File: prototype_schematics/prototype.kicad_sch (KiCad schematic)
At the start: 98 parts, among them J1 AudioJack3, J2 Conn_01x04, J3 Conn_Coaxial, U1 MAX2608EUT+T, U10 TA0411A, U2 SPX3819M5-L, U3 TLV61046ADB, U4 MAX2680AUT+, U5 CD74HC4046A, U6 BGA2802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

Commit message: layout wip
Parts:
- J3: footprint Connector_Coaxial:SMA_Wurth_60312002114503_Vertical -> Connector_Coaxial:SMA_Samtec_SMA-J-P-X-ST-EM1_EdgeMount; Digikey (none) -> CON-SMA-EDGE-S-ND
- L12: footprint Inductor_SMD:L_0201_0603Metric_Pad0.64x0.40mm_HandSolder -> Inductor_SMD:L_0603_1608Metric_Pad1.05x0.95mm_HandSolder
- TP1, TP2, TP3, TP4, TP5, TP6: footprint CONMHF1_SMD_T:CONN_CONMHF1-SMD_LNX -> Connector_Coaxial:U.FL_Molex_MCRF_73412-0110_Vertical
- U6: footprint Package_TO_SOT_SMD:SOT-363_SC-70-6 -> Package_TO_SOT_SMD:SOT-363_SC-70-6_Handsoldering
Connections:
- net GND: now also R9.1; no longer R9.2
- net at C10.2, C13.1, L5.1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: no longer R9.1
- net at C9.2: now also U4.1 (LO); no longer TP1.1 (In)
- net at C1.2: now also TP1.1 (In); no longer U4.1 (LO)
- net at C13.2, U5.14 (SigIn): now also R9.2
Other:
- note removed: "Remove 2kR when using TP"
- moved on the sheet: C10, C13, L5, L6, R9, TP1, TP2

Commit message: wip layout
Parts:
- added C40: 1nF, Capacitor_SMD:C_0603_1608Metric_Pad1.08x0.95mm_HandSolder, symbol Device:C_Small
- J2: footprint Connector_JST:JST_PH_S4B-PH-K_1x04_P2.00mm_Horizontal -> Connector_PinHeader_2.54mm:PinHeader_1x04_P2.54mm_Vertical
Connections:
- net AFOUT_N: now also J2.3 (Pin_3); no longer J2.4 (Pin_4)
- net AFOUT_P: now also J2.4 (Pin_4); no longer J2.3 (Pin_3)
- net GND: now also R9.2; no longer R9.1
- net at C10.2, L5.1: now also C40.1; no longer C13.1, Y1.3 (OUT/IN)
- net at R18.1: now also RV3.1; no longer RV3.3
- net at R17.2: now also RV3.3; no longer RV3.1
- net at C13.2, U5.14 (SigIn): no longer R9.2
- new net: C13.1, C40.2, R9.1, Y1.3 (OUT/IN)
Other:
- moved on the sheet: C10, C13, L5, L6, R9, TP2

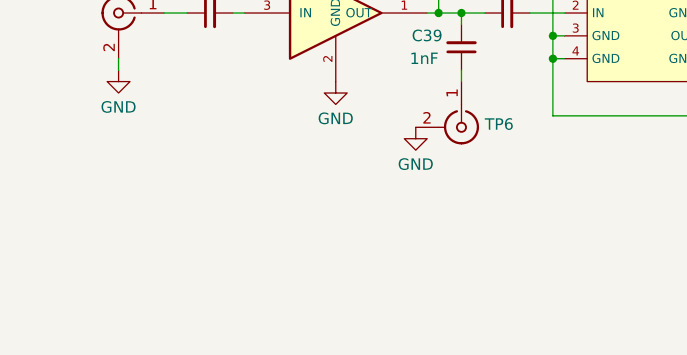
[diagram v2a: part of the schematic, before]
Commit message: layout adjustment and edge cut
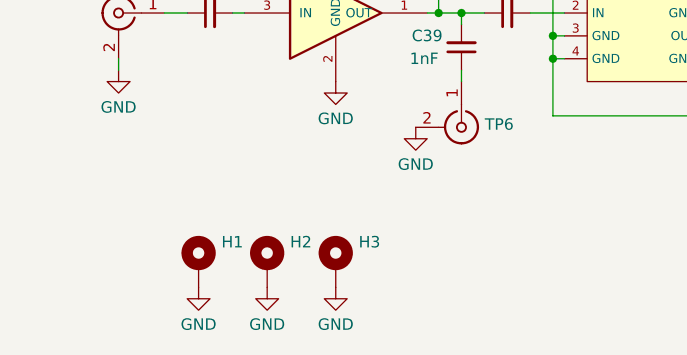
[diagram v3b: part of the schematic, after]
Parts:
- added H1, H2, H3: MountingHole_Pad, MountingHole:MountingHole_3.2mm_M3_Pad_TopBottom, symbol Mechanical:MountingHole_Pad
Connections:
- net GND: now also H1.1, H2.1, H3.1
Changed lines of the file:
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@@
     )
   )
+  (symbol (lib_id "Mechanical:MountingHole_Pad") (at 48.26 187.96 0) (unit 1)
+    (in_bom yes) (on_board yes) (dnp no) (fields_autoplaced)
+    (property "Reference" "H3" (at 50.8 185.4779 0)
+      (effects (font (size 1.27 1.27)) (justify left))
+    )
+    (property "Value" "MountingHole_Pad" (at 50.8 187.9021 0)
+      (effects (font (size 1.27 1.27)) (justify left) hide)
+    )
+    (property "Footprint" "MountingHole:MountingHole_3.2mm_M3_Pad_TopBottom" (at 48.26 187.96 0)
+      (effects (font (size 1.27 1.27)) hide)
+    )
+    (property "Datasheet" "~" (at 48.26 187.96 0)
+      (effects (font (size 1.27 1.27)) hide)
+    )
+    (pin "1")
+    (instances
+      (project "prototype"
+        (path "/4c96c703-bc8d-4d6a-931f-53feb2017a98"
+          (reference "H3") (unit 1)
+        )
+      )
+    )
+  )
   (symbol (lib_id "power:GND") (at 265.43 99.06 0) (unit 1)
     (in_bom yes) (on_board yes) (dnp no) (fields_autoplaced)
@@
     )
   )
+  (symbol (lib_id "power:GND") (at 48.26 190.5 0) (unit 1)
+    (in_bom yes) (on_board yes) (dnp no) (fields_autoplaced)
+    (property "Reference" "#PWR053" (at 48.26 196.85 0)
+      (effects (font (size 1.27 1.27)) hide)
+    )
+    (property "Value" "GND" (at 48.26 194.6331 0)
+      (effects (font (size 1.27 1.27)))
+    )
+    (property "Footprint" "" (at 48.26 190.5 0)
+      (effects (font (size 1.27 1.27)) hide)
+    )
+    (property "Datasheet" "" (at 48.26 190.5 0)
+      (effects (font (size 1.27 1.27)) hide)
+    )
+    (pin "1")
+    (instances
+      (project "prototype"
+        (path "/4c96c703-bc8d-4d6a-931f-53feb2017a98"
+          (reference "#PWR053") (unit 1)
+        )
+      )
+    )
+  )
   (symbol (lib_id "Device:R_Potentiometer_US") (at 25.4 39.37 0) (unit 1)
     (in_bom yes) (on_board yes) (dnp no) (fields_autoplaced)
@@
     )
   )
+  (symbol (lib_id "power:GND") (at 33.02 190.5 0) (unit 1)
+    (in_bom yes) (on_board yes) (dnp no) (fields_autoplaced)
+    (property "Reference" "#PWR051" (at 33.02 196.85 0)
+      (effects (font (size 1.27 1.27)) hide)
+    )
+    (property "Value" "GND" (at 33.02 194.6331 0)
+      (effects (font (size 1.27 1.27)))
+    )
+    (property "Footprint" "" (at 33.02 190.5 0)
+      (effects (font (size 1.27 1.27)) hide)
+    )
+    (property "Datasheet" "" (at 33.02 190.5 0)
+      (effects (font (size 1.27 1.27)) hide)
+    )
+    (pin "1")
+    (instances
+      (project "prototype"
+        (path "/4c96c703-bc8d-4d6a-931f-53feb2017a98"
+          (reference "#PWR051") (unit 1)
+        )
+      )
+    )
+  )
   (symbol (lib_id "Device:R_US") (at 190.5 125.73 0) (unit 1)
     (in_bom yes) (on_board yes) (dnp no) (fields_autoplaced)
@@
     )
   )
+  (symbol (lib_id "power:GND") (at 40.64 190.5 0) (unit 1)
+    (in_bom yes) (on_board yes) (dnp no) (fields_autoplaced)
+    (property "Reference" "#PWR052" (at 40.64 196.85 0)
+      (effects (font (size 1.27 1.27)) hide)
+    )
+    (property "Value" "GND" (at 40.64 194.6331 0)
+      (effects (font (size 1.27 1.27)))
+    )
+    (property "Footprint" "" (at 40.64 190.5 0)
+      (effects (font (size 1.27 1.27)) hide)
+    )
+    (property "Datasheet" "" (at 40.64 190.5 0)
+      (effects (font (size 1.27 1.27)) hide)
+    )
+    (pin "1")
+    (instances
+      (project "prototype"
+        (path "/4c96c703-bc8d-4d6a-931f-53feb2017a98"
+          (reference "#PWR052") (unit 1)
+        )
+      )
+    )
+  )
   (symbol (lib_id "power:GND") (at 231.14 104.14 0) (unit 1)
     (in_bom yes) (on_board yes) (dnp no) (fields_autoplaced)
@@
     )
   )
+  (symbol (lib_id "Mechanical:MountingHole_Pad") (at 33.02 187.96 0) (unit 1)
+    (in_bom yes) (on_board yes) (dnp no) (fields_autoplaced)
+    (property "Reference" "H1" (at 35.56 185.4779 0)
+      (effects (font (size 1.27 1.27)) (justify left))
+    )
+    (property "Value" "MountingHole_Pad" (at 35.56 187.9021 0)
+      (effects (font (size 1.27 1.27)) (justify left) hide)
+    )
+    (property "Footprint" "MountingHole:MountingHole_3.2mm_M3_Pad_TopBottom" (at 33.02 187.96 0)
+      (effects (font (size 1.27 1.27)) hide)
+    )
+    (property "Datasheet" "~" (at 33.02 187.96 0)
+      (effects (font (size 1.27 1.27)) hide)
+    )
+    (pin "1")
+    (instances
+      (project "prototype"
+        (path "/4c96c703-bc8d-4d6a-931f-53feb2017a98"
+          (reference "H1") (unit 1)
+        )
+      )
+    )
+  )
   (symbol (lib_id "Device:R_US") (at 190.5 107.95 0) (unit 1)
     (in_bom yes) (on_board yes) (dnp no) (fields_autoplaced)
@@
         )
       )
+    )
+  )
+  (symbol (lib_id "Mechanical:MountingHole_Pad") (at 40.64 187.96 0) (unit 1)
+    (in_bom yes) (on_board yes) (dnp no) (fields_autoplaced)
+    (property "Reference" "H2" (at 43.18 185.4779 0)
+      (effects (font (size 1.27 1.27)) (justify left))
+    )
+    (property "Value" "MountingHole_Pad" (at 43.18 187.9021 0)
+      (effects (font (size 1.27 1.27)) (justify left) hide)
+    )
+    (property "Footprint" "MountingHole:MountingHole_3.2mm_M3_Pad_TopBottom" (at 40.64 187.96 0)
+      (effects (font (size 1.27 1.27)) hide)
+    )
+    (property "Datasheet" "~" (at 40.64 187.96 0)
+      (effects (font (size 1.27 1.27)) hide)
+    )
+    (pin "1")
+    (instances
+      (project "prototype"
+        (path "/4c96c703-bc8d-4d6a-931f-53feb2017a98"
+          (reference "H2") (unit 1)
+        )
+      )

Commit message: finish routing
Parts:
- added H4: MountingHole_Pad, MountingHole:MountingHole_3.2mm_M3_Pad_TopBottom, symbol Mechanical:MountingHole_Pad
- J1: footprint SJ1_2503A:CONN_SJ1-2503A -> SJ1_2503A:CUI_SJ1-2503A
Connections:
- net AFOUT_N: now also J2.4 (Pin_4); no longer J2.3 (Pin_3)
- net AFOUT_P: now also J2.3 (Pin_3); no longer J2.4 (Pin_4)
- net GND: now also H4.1
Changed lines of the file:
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@@
     (effects (font (size 1 1)) (justify left bottom))
   )
-  (label "AFOUT_N" (at 189.23 156.21 0) (fields_autoplaced)
+  (label "AFOUT_N" (at 189.23 158.75 0) (fields_autoplaced)
     (effects (font (size 1.27 1.27)) (justify left bottom))
   )
@@
     (effects (font (size 1.27 1.27)) (justify left bottom))
   )
-  (label "AFOUT_P" (at 189.23 158.75 0) (fields_autoplaced)
+  (label "AFOUT_P" (at 189.23 156.21 0) (fields_autoplaced)
     (effects (font (size 1.27 1.27)) (justify left bottom))
   )
@@
     )
   )
+  (symbol (lib_id "power:GND") (at 55.88 190.5 0) (unit 1)
+    (in_bom yes) (on_board yes) (dnp no) (fields_autoplaced)
+    (property "Reference" "#PWR054" (at 55.88 196.85 0)
+      (effects (font (size 1.27 1.27)) hide)
+    )
+    (property "Value" "GND" (at 55.88 194.6331 0)
+      (effects (font (size 1.27 1.27)))
+    )
+    (property "Footprint" "" (at 55.88 190.5 0)
+      (effects (font (size 1.27 1.27)) hide)
+    )
+    (property "Datasheet" "" (at 55.88 190.5 0)
+      (effects (font (size 1.27 1.27)) hide)
+    )
+    (pin "1")
+    (instances
+      (project "prototype"
+        (path "/4c96c703-bc8d-4d6a-931f-53feb2017a98"
+          (reference "#PWR054") (unit 1)
+        )
+      )
+    )
+  )
   (symbol (lib_id "Connector_Generic:Conn_01x04") (at 184.15 153.67 0) (mirror y) (unit 1)
     (in_bom yes) (on_board yes) (dnp no) (fields_autoplaced)
@@
     )
   )
+  (symbol (lib_id "Mechanical:MountingHole_Pad") (at 55.88 187.96 0) (unit 1)
+    (in_bom yes) (on_board yes) (dnp no) (fields_autoplaced)
+    (property "Reference" "H4" (at 58.42 185.4779 0)
+      (effects (font (size 1.27 1.27)) (justify left))
+    )
+    (property "Value" "MountingHole_Pad" (at 58.42 187.9021 0)
+      (effects (font (size 1.27 1.27)) (justify left) hide)
+    )
+    (property "Footprint" "MountingHole:MountingHole_3.2mm_M3_Pad_TopBottom" (at 55.88 187.96 0)
+      (effects (font (size 1.27 1.27)) hide)
+    )
+    (property "Datasheet" "~" (at 55.88 187.96 0)
+      (effects (font (size 1.27 1.27)) hide)
+    )
+    (pin "1")
+    (instances
+      (project "prototype"
+        (path "/4c96c703-bc8d-4d6a-931f-53feb2017a98"
+          (reference "H4") (unit 1)
+        )
+      )
+    )
+  )
   (symbol (lib_id "Device:R_US") (at 147.32 43.18 0) (unit 1)
     (in_bom yes) (on_board yes) (dnp no) (fields_autoplaced)
@@
       (effects (font (size 1.27 1.27)) (justify right) hide)
     )
-    (property "Footprint" "SJ1_2503A:CONN_SJ1-2503A" (at 246.38 114.3 0)
+    (property "Footprint" "SJ1_2503A:CUI_SJ1-2503A" (at 246.38 114.3 0)
       (effects (font (size 1.27 1.27)) hide)
     )

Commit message: add a few more gnd vias
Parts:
- J3: Digikey CON-SMA-EDGE-S-ND -> 931-1175-ND
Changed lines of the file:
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@@
       (effects (font (size 1.27 1.27)) hide)
     )
-    (property "Digikey" "CON-SMA-EDGE-S-ND" (at 24.13 160.02 0)
+    (property "Digikey" "931-1175-ND" (at 24.13 160.02 0)
       (effects (font (size 1.27 1.27)) hide)
     )
